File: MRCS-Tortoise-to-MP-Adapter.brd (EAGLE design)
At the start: 44.5 x 31.8 mm, 6 parts, among them K1 G6H2-100

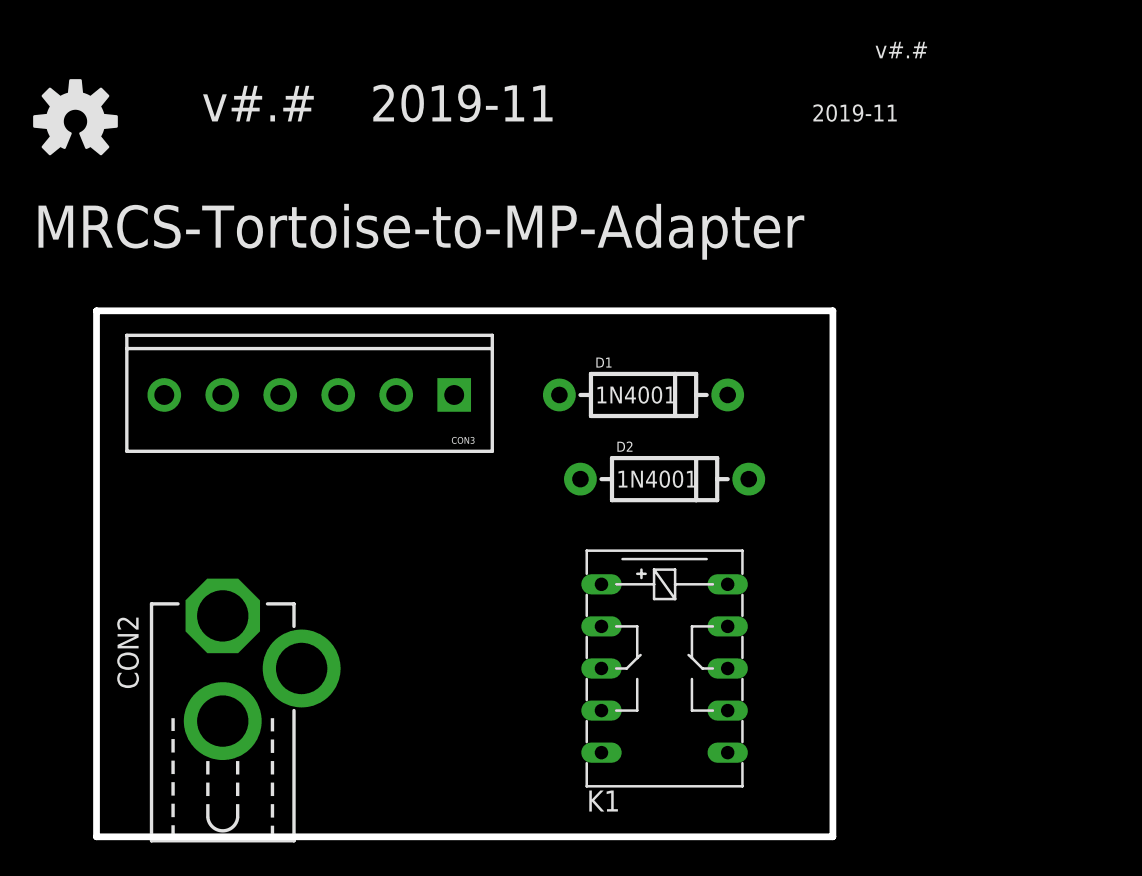
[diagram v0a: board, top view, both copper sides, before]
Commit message: clean up in preparation for panelization
1st rev worked well and seems OK, add Prop 65 warning and minor label cleanup
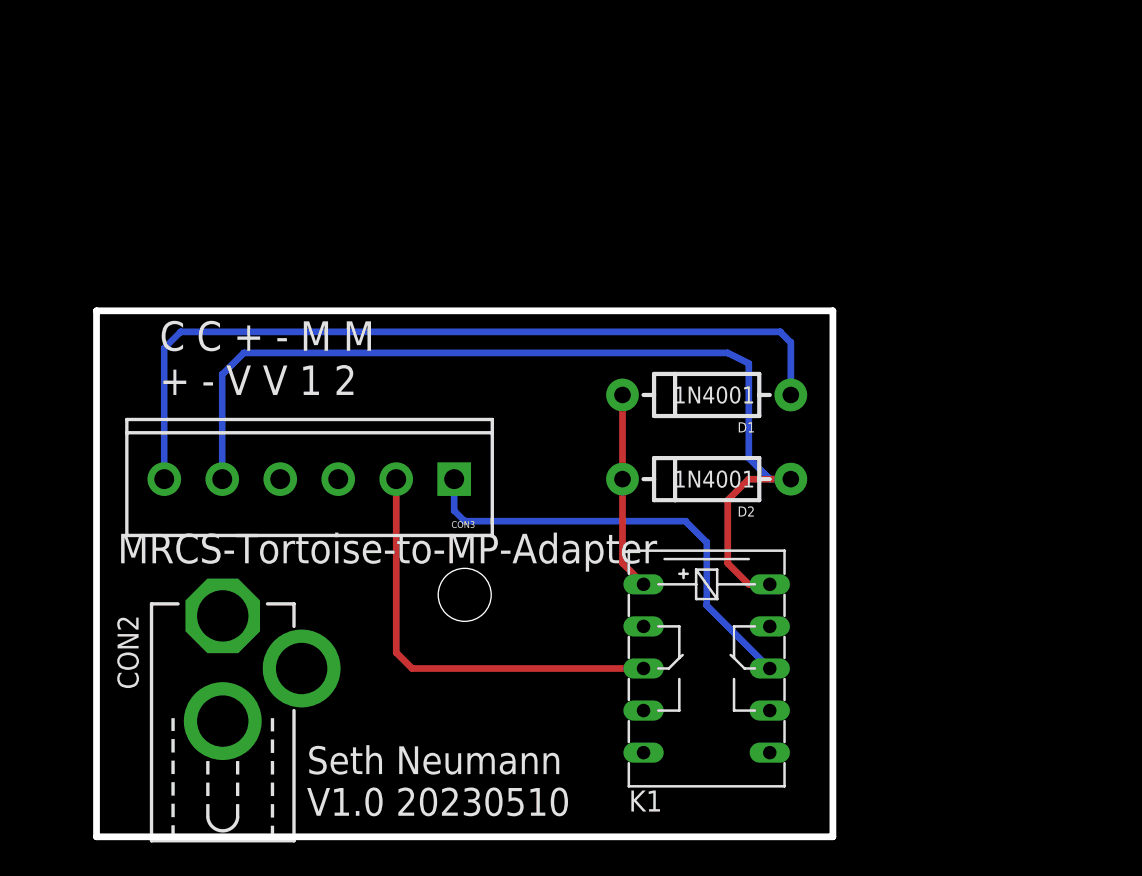
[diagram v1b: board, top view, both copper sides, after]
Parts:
- removed OSHW1: DOC-OSHW-LOGO-M, SPCoast:OSHW-LOGO-M
- added U$1: (no value), MRCSLogoTop:MRCSLOGOTOP
- added U$2: (no value), MRCS-prop65warningBtm:CA-PROP65WARNING
- added U$3: (no value), MRCSLogoBtm:MRCSLOGOBTM
- moved CON3 5.08 mm to (21.6, 21.6)
- moved D1 3.81 mm to (36.8, 26.7), turned to 0 degrees
- moved D2 2.54 mm to (36.8, 21.6), turned to 0 degrees
- moved K1 2.54 mm to (36.8, 10.2)
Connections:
- net N$4 renamed VIN
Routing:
- net N$3: track 0.00 -> 58.8 mm
- net N$1: track 0.00 -> 49.6 mm
- net N$7: track 0.00 -> 27.1 mm
- net N$6: track 0.00 -> 25.8 mm
- net N$2: track 0.00 -> 12.0 mm
- added copper zone on layer 16, net GND
- added copper zone on layer 1, net VIN
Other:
- board text added: "C C + - M M + - V V 1 2"
- board text added: "Seth Neumann V1.0 20230510"
- board text removed: "2019-11"
- board text removed: "v#.#"
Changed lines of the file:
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@@
 <board>
 <plain>
-<text x="-3.81" y="35.56" size="2.54" layer="21" font="vector" ratio="10">&gt;DRAWING_NAME </text>
-<text x="6.35" y="43.18" size="2.1844" layer="21" font="vector" ratio="10">v#.#</text>
-<text x="16.51" y="43.18" size="2.1844" layer="21" font="vector" ratio="10">2019-11</text>
-<text x="40.64" y="49.53" size="1.778" layer="21" font="vector" ratio="10" rot="R180">&gt;DRAWING_NAME </text>
-<text x="43.18" y="43.18" size="1.016" layer="21" font="vector" ratio="10">2019-11</text>
-<text x="46.99" y="46.99" size="1.016" layer="21" font="vector" ratio="10">v#.#</text>
+<text x="1.27" y="16.51" size="1.778" layer="21" font="vector" ratio="10">&gt;DRAWING_NAME </text>
+<text x="1.27" y="3.81" size="1.778" layer="22" font="vector" ratio="10" rot="MR180">&gt;DRAWING_NAME </text>
 <wire x1="0" y1="0" x2="44.45" y2="0" width="0.4064" layer="20"/>
 <wire x1="44.45" y1="0" x2="44.45" y2="31.75" width="0.4064" layer="20"/>
 <wire x1="44.45" y1="31.75" x2="0" y2="31.75" width="0.4064" layer="20"/>
 <wire x1="0" y1="31.75" x2="0" y2="0" width="0.4064" layer="20"/>
+<text x="12.7" y="1.27" size="1.6764" layer="21" font="vector" ratio="10">Seth Neumann
+V1.0 20230510</text>
+<hole x="22.225" y="14.605" drill="3.2"/>
+<text x="3.81" y="26.67" size="1.778" layer="21" font="vector" ratio="10">C C + - M M
++ - V V 1 2</text>
 </plain>
 <attributes>
@@
 </autorouter>
 <elements>
-<element name="OSHW1" library="SPCoast" package="OSHW-LOGO-M" value="DOC-OSHW-LOGO-M" x="-1.27" y="43.18"/>
-<element name="K1" library="relay" package="G6H2-100" value="G6H2-100" x="34.29" y="10.16" rot="R270">
-<attribute name="OC_NEWARK" value="unknown" x="34.29" y="10.16" size="1.778" layer="27" font="vector" ratio="10" rot="R270" display="off"/>
-<attribute name="MF" value="" x="34.29" y="10.16" size="1.778" layer="27" font="vector" ratio="10" rot="R270" display="off"/>
-<attribute name="OC_FARNELL" value="unknown" x="34.29" y="10.16" size="1.778" layer="27" font="vector" ratio="10" rot="R270" display="off"/>
-<attribute name="MPN" value="" x="34.29" y="10.16" size="1.778" layer="27" font="vector" ratio="10" rot="R270" display="off"/>
+<element name="K1" library="relay" package="G6H2-100" value="G6H2-100" x="36.83" y="10.16" smashed="yes" rot="R270">
+<attribute name="OC_NEWARK" value="unknown" x="36.83" y="10.16" size="1.778" layer="27" font="vector" ratio="10" rot="R270" display="off"/>
+<attribute name="MF" value="" x="36.83" y="10.16" size="1.778" layer="27" font="vector" ratio="10" rot="R270" display="off"/>
+<attribute name="OC_FARNELL" value="unknown" x="36.83" y="10.16" size="1.778" layer="27" font="vector" ratio="10" rot="R270" display="off"/>
+<attribute name="MPN" value="" x="36.83" y="10.16" size="1.778" layer="27" font="vector" ratio="10" rot="R270" display="off"/>
+<attribute name="NAME" x="32.131" y="1.524" size="1.27" layer="25" ratio="10"/>
+<attribute name="VALUE" x="36.195" y="15.24" size="1.27" layer="27" ratio="10" rot="R270"/>
 </element>
-<element name="D1" library="SPCoast" package="DIODE-1N4001" value="1N4001" x="33.02" y="26.67" rot="R180"/>
+<element name="D1" library="SPCoast" package="DIODE-1N4001" value="1N4001" x="36.83" y="26.67"/>
 <element name="CON2" library="SPCoast" package="DCJ0202" value="" x="7.62" y="10.16"/>
-<element name="CON3" library="SPCoast" package="SCREWTERMINAL-3.5MM-6" value="" x="21.59" y="26.67" rot="R180"/>
-<element name="D2" library="SPCoast" package="DIODE-1N4001" value="1N4001" x="34.29" y="21.59" rot="R180"/>
+<element name="CON3" library="SPCoast" package="SCREWTERMINAL-3.5MM-6" value="" x="21.59" y="21.59" rot="R180"/>
+<element name="D2" library="SPCoast" package="DIODE-1N4001" value="1N4001" x="36.83" y="21.59"/>
+<element name="U$1" library="MRCSLogoTop" package="MRCSLOGOTOP" value="" x="18.415" y="6.35"/>
+<element name="U$2" library="MRCS-prop65warningBtm" package="CA-PROP65WARNING" value="" x="24.13" y="26.67"/>
+<element name="U$3" library="MRCSLogoBtm" package="MRCSLOGOBTM" value="" x="22.86" y="6.35"/>
 </elements>
 <signals>
@@
 <contactref element="CON3" pad="6"/>
 <contactref element="D1" pad="A"/>
-<wire x1="4.09" y1="26.67" x2="27.94" y2="26.67" width="0" layer="19" extent="1-1"/>
+<wire x1="41.91" y1="26.67" x2="41.91" y2="29.845" width="0.4064" layer="16"/>
+<wire x1="41.91" y1="29.845" x2="41.275" y2="30.48" width="0.4064" layer="16"/>
+<wire x1="41.275" y1="30.48" x2="5.08" y2="30.48" width="0.4064" layer="16"/>
+<wire x1="4.09" y1="21.59" x2="4.09" y2="29.49" width="0.4064" layer="16"/>
+<wire x1="4.09" y1="29.49" x2="5.08" y2="30.48" width="0.4064" layer="16"/>
 </signal>
 <signal name="N$2">
@@
 <contactref element="K1" pad="1"/>
 <contactref element="D2" pad="C"/>
-<wire x1="30.48" y1="15.24" x2="38.1" y2="26.67" width="0" layer="19" extent="1-1"/>
-<wire x1="39.37" y1="21.59" x2="30.48" y2="15.24" width="0" layer="19" extent="1-1"/>
+<wire x1="31.75" y1="26.67" x2="31.75" y2="21.59" width="0.4064" layer="1"/>
+<wire x1="31.75" y1="21.59" x2="31.75" y2="16.51" width="0.4064" layer="1"/>
+<wire x1="31.75" y1="16.51" x2="33.02" y2="15.24" width="0.4064" layer="1"/>
 </signal>
 <signal name="N$3">
@@
 <contactref element="CON3" pad="5"/>
 <contactref element="D2" pad="A"/>
-<wire x1="7.59" y1="26.67" x2="38.1" y2="15.24" width="0" layer="19" extent="1-1"/>
-<wire x1="29.21" y1="21.59" x2="7.59" y2="26.67" width="0" layer="19" extent="1-1"/>
-</signal>
-<signal name="N$4">
-<contactref element="CON3" pad="4"/>
-<contactref element="K1" pad="O1"/>
-<contactref element="K1" pad="S2"/>
-<contactref element="CON2" pad="1"/>
-<wire x1="30.48" y1="12.7" x2="38.1" y2="7.62" width="0" layer="19" extent="1-1"/>
-<wire x1="7.62" y1="13.335" x2="30.48" y2="12.7" width="0" layer="19" extent="1-1"/>
-<wire x1="11.09" y1="26.67" x2="7.62" y2="13.335" width="0" layer="19" extent="1-1"/>
+<wire x1="7.59" y1="21.59" x2="7.59" y2="27.91" width="0.4064" layer="16"/>
+<wire x1="7.59" y1="27.91" x2="8.89" y2="29.21" width="0.4064" layer="16"/>
+<wire x1="8.89" y1="29.21" x2="38.1" y2="29.21" width="0.4064" layer="16"/>
+<wire x1="38.1" y1="29.21" x2="39.37" y2="28.575" width="0.4064" layer="16"/>
+<wire x1="39.37" y1="28.575" x2="39.37" y2="22.86" width="0.4064" layer="16"/>
+<wire x1="39.37" y1="22.86" x2="40.64" y2="21.59" width="0.4064" layer="16"/>
+<wire x1="40.64" y1="21.59" x2="41.91" y2="21.59" width="0.4064" layer="16"/>
+<wire x1="40.64" y1="15.24" x2="39.37" y2="15.24" width="0.4064" layer="1"/>
+<wire x1="39.37" y1="15.24" x2="38.1" y2="16.51" width="0.4064" layer="1"/>
+<wire x1="38.1" y1="16.51" x2="38.1" y2="20.32" width="0.4064" layer="1"/>
+<wire x1="38.1" y1="20.32" x2="39.37" y2="21.59" width="0.4064" layer="1"/>
+<wire x1="39.37" y1="21.59" x2="41.91" y2="21.59" width="0.4064" layer="1"/>
 </signal>
 <signal name="N$6">
 <contactref element="CON3" pad="2"/>
+<wire x1="18.09" y1="21.59" x2="18.09" y2="11.12" width="0.4064" layer="1"/>
+<wire x1="18.09" y1="11.12" x2="19.05" y2="10.16" width="0.4064" layer="1"/>
 <contactref element="K1" pad="P1"/>
-<wire x1="18.09" y1="26.67" x2="30.48" y2="10.16" width="0" layer="19" extent="1-1"/>
+<wire x1="19.05" y1="10.16" x2="33.02" y2="10.16" width="0.4064" layer="1"/>
 </signal>
 <signal name="N$7">
 <contactref element="CON3" pad="1"/>
 <contactref element="K1" pad="P2"/>
-<wire x1="21.59" y1="26.67" x2="38.1" y2="10.16" width="0" layer="19" extent="1-1"/>
+<wire x1="40.64" y1="10.16" x2="36.83" y2="13.97" width="0.4064" layer="16"/>
+<wire x1="22.225" y1="19.05" x2="21.59" y2="19.685" width="0.4064" layer="16"/>
+<wire x1="21.59" y1="19.685" x2="21.59" y2="21.59" width="0.4064" layer="16"/>
+<wire x1="22.225" y1="19.05" x2="35.56" y2="19.05" width="0.4064" layer="16"/>
+<wire x1="35.56" y1="19.05" x2="36.83" y2="17.78" width="0.4064" layer="16"/>
+<wire x1="36.83" y1="17.78" x2="36.83" y2="13.97" width="0.4064" layer="16"/>
 </signal>
 <signal name="GND">
 <contactref element="CON2" pad="2"/>
 <contactref element="CON2" pad="3"/>
+<polygon width="0.4064" layer="16">
+<vertex x="0" y="0"/>
+<vertex x="44.45" y="0"/>
+<vertex x="44.45" y="31.75"/>
+<vertex x="0" y="31.75"/>
+</polygon>
 <contactref element="CON3" pad="3"/>
+<contactref element="K1" pad="O2"/>
 <contactref element="K1" pad="S1"/>
-<contactref element="K1" pad="O2"/>
-<wire x1="30.48" y1="7.62" x2="38.1" y2="12.7" width="0" layer="19" extent="1-1"/>
-<wire x1="12.3825" y1="10.16" x2="30.48" y2="7.62" width="0" layer="19" extent="1-1"/>
-<wire x1="7.62" y1="6.985" x2="12.3825" y2="10.16" width="0" layer="19" extent="1-1"/>
-<wire x1="14.59" y1="26.67" x2="7.62" y2="6.985" width="0" layer="19" extent="1-1"/>
+</signal>
+<signal name="VIN">
+<contactref element="CON3" pad="4"/>
+<contactref element="K1" pad="S2"/>
+<contactref element="CON2" pad="1"/>
+<contactref element="K1" pad="O1"/>
+<polygon width="0.4064" layer="1">
+<vertex x="0" y="0"/>
+<vertex x="44.45" y="0"/>
+<vertex x="44.45" y="31.75"/>
+<vertex x="0" y="31.75"/>
+</polygon>
 </signal>
 </signals>
 </board>
 </drawing>
+<compatibility>
+<note version="6.3" minversion="6.2.2" severity="warning">
+Since Version 6.2.2 text objects can contain more than one line,
+which will not be processed correctly with this version.
+</note>
+</compatibility>
 </eagle>
